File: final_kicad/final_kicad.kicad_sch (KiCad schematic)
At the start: 70 parts, among them J3 Reflectance Sensor Array, M1 Motor, M3 Servo for Side Indicator, M4 Servo for Gripper, M5 Motor_Step_4Wire, M6 Motor for Linear Actuator, Q1 Photo_NPN, Q2 MOSFET-N, SW1 Reset, SW2 Reset, U1 SN754410, U2 MCP6294, U2 PIC32MX170F256B, U4 Comparator, U5 L293NE, U6 L293NE

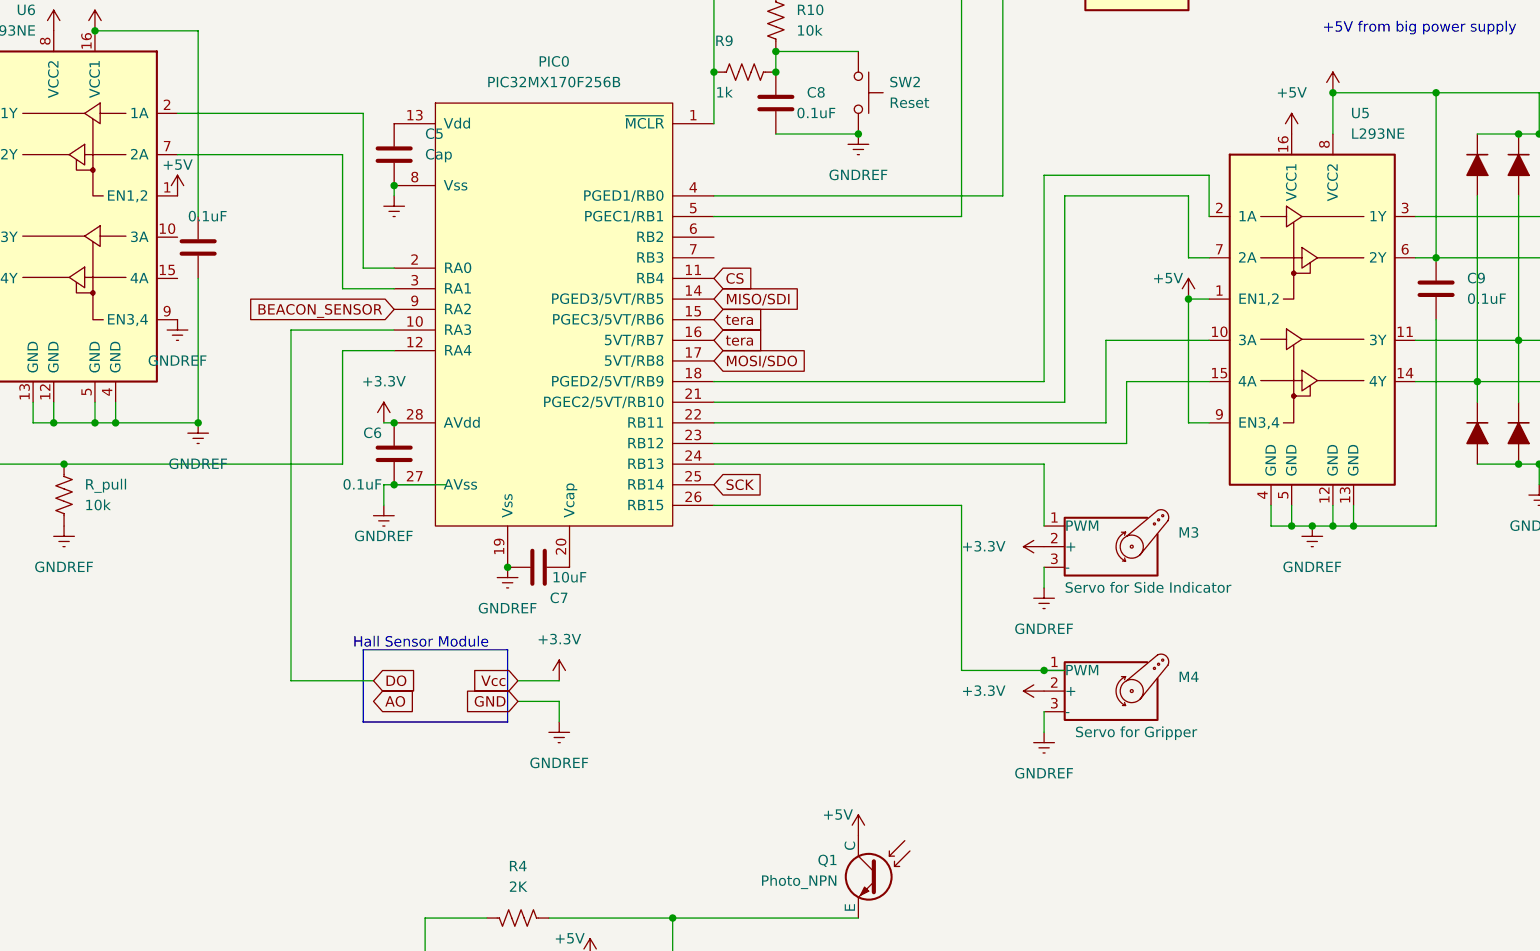
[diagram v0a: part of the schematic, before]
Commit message: update kicad with arm motors
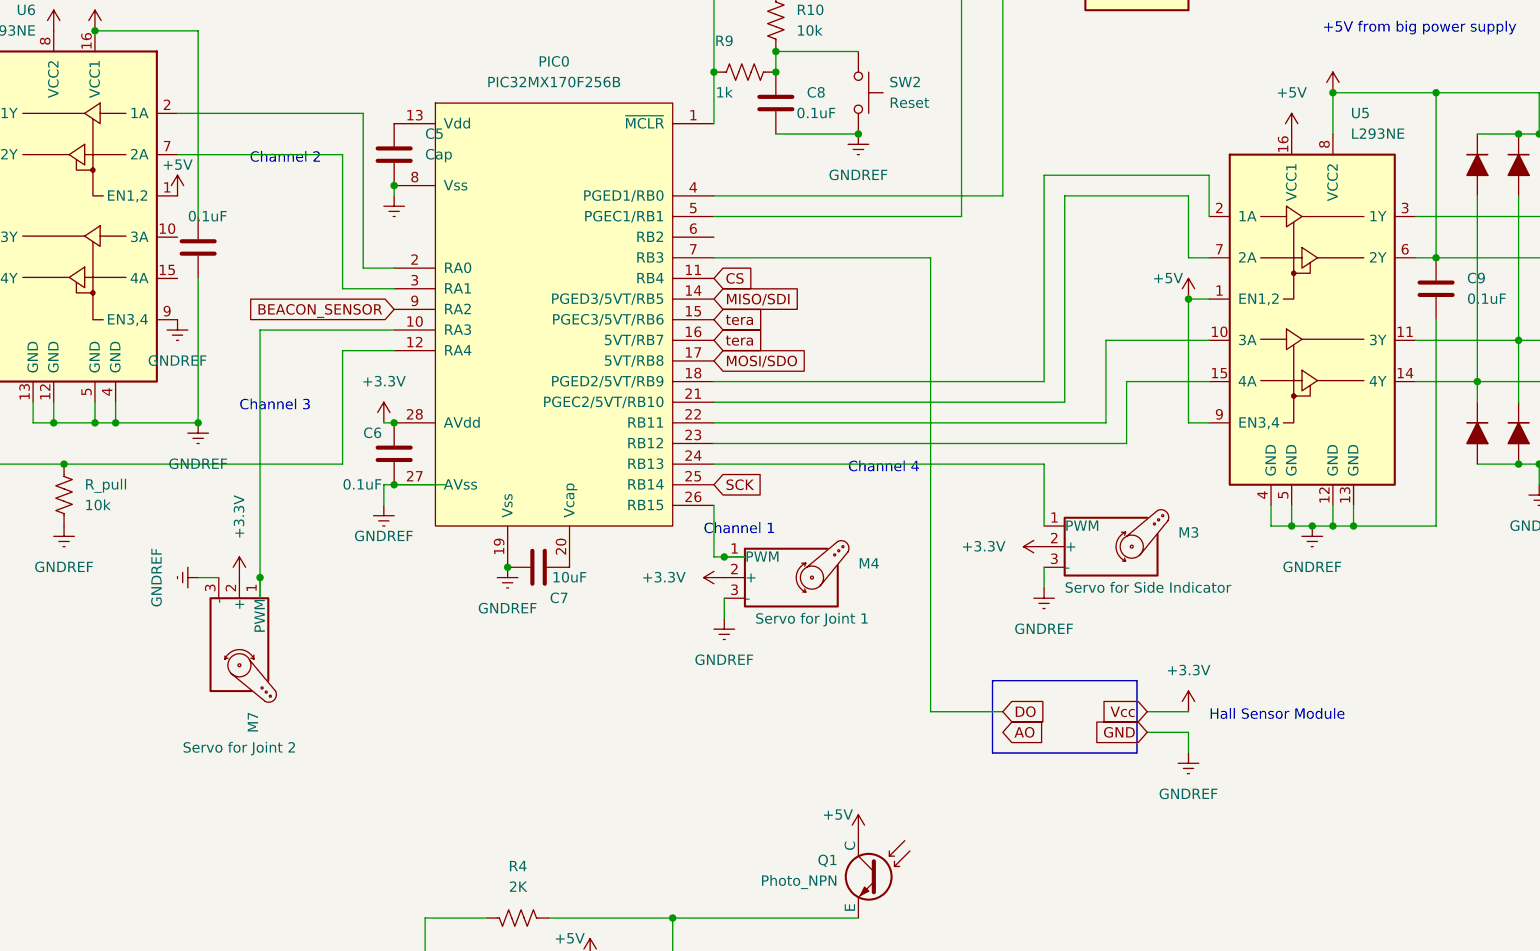
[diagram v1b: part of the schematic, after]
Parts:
- added M7: Servo for Joint 2, symbol ME218_BaseLib:Motor_Servo
- M4: value Servo for Gripper -> Servo for Joint 1
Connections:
- net +3.3V: now also M7.2 (+)
- net DO: now also PIC0.7 (RB3); no longer PIC0.10 (RA3)
- net GND: now also M7.3 (-)
- new net: M7.1 (PWM), PIC0.10 (RA3)
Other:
- note added: "Channel 1"
- note added: "Channel 2"
- note added: "Channel 3"
- note added: "Channel 4"
- moved on the sheet: M4
